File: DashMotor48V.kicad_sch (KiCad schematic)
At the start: 79 parts, among them CN3(OUT)1 XT30(2+2)PB-M.G.B, CN3(OUT)2 XT30(2+2)PB-M.G.B, J1 BM07B-SRSS-TB, J2 BM07B-SRSS-TB, Q1 FDMS039N08B, Q2 FDMS039N08B, Q3 FDMS039N08B, Q4 FDMS039N08B, Q5 FDMS039N08B, Q6 FDMS039N08B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

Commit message: Add files via upload
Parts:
- removed H1, H2, H3: MountingHole_Pad, MountingHole:MountingHole_2.2mm_M2_Pad, symbol Mechanical:MountingHole_Pad
- added H1, H2, H3: Phase A, dash:Pad_Square_Vias_6.5x6.5mm, symbol 0_connectors:Solder Pad
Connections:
- net PHASA: now also H1.1
- net PHASB: now also H2.1
- net PHASC: now also H3.1
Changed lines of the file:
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@@
 	)
 	(symbol
+		(lib_id "0_connectors:Solder Pad")
+		(at 499.11 104.14 270)
+		(unit 1)
+		(exclude_from_sim no)
+		(in_bom no)
+		(on_board yes)
+		(dnp no)
+		(property "Reference" "H3"
+			(at 503.555 97.79 90)
+			(effects
+				(font
+					(size 1.27 1.27)
+				)
+			)
+		)
+		(property "Value" "Phase A"
+			(at 503.555 100.33 90)
+			(effects
+				(font
+					(size 1.27 1.27)
+				)
+			)
+		)
+		(property "Footprint" "dash:Pad_Square_Vias_6.5x6.5mm"
+			(at 499.11 109.22 0)
+			(effects
+				(font
+					(size 1.27 1.27)
+				)
+				(hide yes)
+			)
+		)
+		(property "Datasheet" "~"
+			(at 499.11 109.22 0)
+			(effects
+				(font
+					(size 1.27 1.27)
+				)
+				(hide yes)
+			)
+		)
+		(property "Description" ""
+			(at 499.11 104.14 0)
+			(effects
+				(font
+					(size 1.27 1.27)
+				)
+				(hide yes)
+			)
+		)
+		(pin "1"
+		)
+		(instances
+			(project "DashMotor48V"
+				(path "/71f0fcc1-c7ad-470c-8d48-d038c53969d3"
+					(reference "H3")
+					(unit 1)
+				)
+			)
+		)
+	)
+	(symbol
 		(lib_id "dash:GRM32EC72A106KE05L")
 		(at 400.05 49.53 90)
@@
 	)
 	(symbol
-		(lib_id "Mechanical:MountingHole_Pad")
-		(at 499.11 101.6 0)
-		(unit 1)
-		(exclude_from_sim no)
-		(in_bom no)
-		(on_board yes)
-		(dnp no)
-		(fields_autoplaced yes)
-		(property "Reference" "H3"
-			(at 501.65 99.0599 0)
-			(effects
-				(font
-					(size 1.27 1.27)
-				)
-				(justify left)
-			)
-		)
-		(property "Value" "MountingHole_Pad"
-			(at 501.65 101.5999 0)
-			(effects
-				(font
-					(size 1.27 1.27)
-				)
-				(justify left)
-				(hide yes)
-			)
-		)
-		(property "Footprint" "MountingHole:MountingHole_2.2mm_M2_Pad"
-			(at 499.11 101.6 0)
-			(effects
-				(font
-					(size 1.27 1.27)
-				)
-				(hide yes)
-			)
-		)
-		(property "Datasheet" "~"
-			(at 499.11 101.6 0)
-			(effects
-				(font
-					(size 1.27 1.27)
-				)
-				(hide yes)
-			)
-		)
-		(property "Description" "Mounting Hole with connection"
-			(at 499.11 101.6 0)
-			(effects
-				(font
-					(size 1.27 1.27)
-				)
-				(hide yes)
-			)
-		)
-		(pin "1"
-		)
-		(instances
-			(project "DashMotor48V"
-				(path "/71f0fcc1-c7ad-470c-8d48-d038c53969d3"
-					(reference "H3")
-					(unit 1)
-				)
-			)
-		)
-	)
-	(symbol
 		(lib_id "power:+12V")
 		(at 398.78 309.88 90)
@@
 	)
 	(symbol
-		(lib_id "Mechanical:MountingHole_Pad")
-		(at 411.48 101.6 0)
+		(lib_id "power:PWR_FLAG")
+		(at 398.78 340.36 270)
 		(unit 1)
 		(exclude_from_sim no)
-		(in_bom no)
+		(in_bom yes)
 		(on_board yes)
 		(dnp no)
 		(fields_autoplaced yes)
-		(property "Reference" "H1"
-			(at 414.02 99.0599 0)
+		(property "Reference" "#FLG05"
+			(at 400.685 340.36 0)
 			(effects
 				(font
 					(size 1.27 1.27)
 				)
-				(justify left)
+				(hide yes)
 			)
 		)
-		(property "Value" "MountingHole_Pad"
-			(at 414.02 101.5999 0)
+		(property "Value" "PWR_FLAG"
+			(at 403.86 340.36 0)
 			(effects
 				(font
 					(size 1.27 1.27)
 				)
-				(justify left)
-				(hide yes)
 			)
 		)
-		(property "Footprint" "MountingHole:MountingHole_2.2mm_M2_Pad"
-			(at 411.48 101.6 0)
+		(property "Footprint" ""
+			(at 398.78 340.36 0)
 			(effects
 				(font
@@
 		)
 		(property "Datasheet" "~"
-			(at 411.48 101.6 0)
+			(at 398.78 340.36 0)
 			(effects
 				(font
@@
 			)
 		)
-		(property "Description" "Mounting Hole with connection"
-			(at 411.48 101.6 0)
+		(property "Description" "Special symbol for telling ERC where power comes from"
+			(at 398.78 340.36 0)
 			(effects
 				(font
@@
 		)
 		(instances
-			(project ""
+			(project "DashMotor48V"
 				(path "/71f0fcc1-c7ad-470c-8d48-d038c53969d3"
-					(reference "H1")
+					(reference "#FLG05")
 					(unit 1)
 				)
@@
 	)
 	(symbol
-		(lib_id "power:PWR_FLAG")
-		(at 398.78 340.36 270)
+		(lib_id "0_connectors:Solder Pad")
+		(at 454.66 104.14 270)
 		(unit 1)
 		(exclude_from_sim no)
-		(in_bom yes)
+		(in_bom no)
 		(on_board yes)
 		(dnp no)
-		(fields_autoplaced yes)
-		(property "Reference" "#FLG05"
-			(at 400.685 340.36 0)
+		(property "Reference" "H2"
+			(at 459.105 97.79 90)
 			(effects
 				(font
 					(size 1.27 1.27)
 				)
-				(hide yes)
 			)
 		)
-		(property "Value" "PWR_FLAG"
-			(at 403.86 340.36 0)
+		(property "Value" "Phase A"
+			(at 459.105 100.33 90)
 			(effects
 				(font
@@
 			)
 		)
-		(property "Footprint" ""
-			(at 398.78 340.36 0)
+		(property "Footprint" "dash:Pad_Square_Vias_6.5x6.5mm"
+			(at 454.66 109.22 0)
 			(effects
 				(font
@@
 		)
 		(property "Datasheet" "~"
-			(at 398.78 340.36 0)
+			(at 454.66 109.22 0)
 			(effects
 				(font
@@
 			)
 		)
-		(property "Description" "Special symbol for telling ERC where power comes from"
-			(at 398.78 340.36 0)
+		(property "Description" ""
+			(at 454.66 104.14 0)
 			(effects
 				(font
@@
 			(project "DashMotor48V"
 				(path "/71f0fcc1-c7ad-470c-8d48-d038c53969d3"
-					(reference "#FLG05")
+					(reference "H2")
 					(unit 1)
 				)
@@
 	)
 	(symbol
-		(lib_id "Mechanical:MountingHole_Pad")
-		(at 454.66 101.6 0)
-		(unit 1)
-		(exclude_from_sim no)
-		(in_bom no)
-		(on_board yes)
-		(dnp no)
-		(fields_autoplaced yes)
-		(property "Reference" "H2"
-			(at 457.2 99.0599 0)
-			(effects
-				(font
-					(size 1.27 1.27)
-				)
-				(justify left)
-			)
-		)
-		(property "Value" "MountingHole_Pad"
-			(at 457.2 101.5999 0)
-			(effects
-				(font
-					(size 1.27 1.27)
-				)
-				(justify left)
-				(hide yes)
-			)
-		)
-		(property "Footprint" "MountingHole:MountingHole_2.2mm_M2_Pad"
-			(at 454.66 101.6 0)
-			(effects
-				(font
-					(size 1.27 1.27)
-				)
-				(hide yes)
-			)
-		)
-		(property "Datasheet" "~"
-			(at 454.66 101.6 0)
-			(effects
-				(font
-					(size 1.27 1.27)
-				)
-				(hide yes)
-			)
-		)
-		(property "Description" "Mounting Hole with connection"
-			(at 454.66 101.6 0)
-			(effects
-				(font
-					(size 1.27 1.27)
-				)
-				(hide yes)
-			)
-		)
-		(pin "1"
-		)
-		(instances
-			(project "DashMotor48V"
-				(path "/71f0fcc1-c7ad-470c-8d48-d038c53969d3"
-					(reference "H2")
-					(unit 1)
-				)
-			)
-		)
-	)
-	(symbol
 		(lib_id "dash:FDMS039N08B")
 		(at 487.68 123.19 0)
@@
 					(unit 1)
 				)
+			)
+		)
+	)
+	(symbol
+		(lib_id "0_connectors:Solder Pad")
+		(at 411.48 104.14 270)
+		(unit 1)
+		(exclude_from_sim no)
+		(in_bom no)
+		(on_board yes)
+		(dnp no)
+		(property "Reference" "H1"
+			(at 415.925 97.79 90)
+			(effects
+				(font
+					(size 1.27 1.27)
+				)
+			)
+		)
+		(property "Value" "Phase A"
+			(at 415.925 100.33 90)
+			(effects
+				(font
+					(size 1.27 1.27)
+				)
+			)
+		)
+		(property "Footprint" "dash:Pad_Square_Vias_6.5x6.5mm"
+			(at 411.48 109.22 0)
+			(effects
+				(font
+					(size 1.27 1.27)
+				)
+				(hide yes)
+			)
+		)
+		(property "Datasheet" "~"
+			(at 411.48 109.22 0)
+			(effects
+				(font
+					(size 1.27 1.27)
+				)
+				(hide yes)
+			)
+		)
+		(property "Description" ""
+			(at 411.48 104.14 0)
+			(effects
+				(font
+					(size 1.27 1.27)
+				)
+				(hide yes)
+			)
+		)
+		(pin "1"
+		)
+		(instances
+			(project "DashMotor48V"
+				(path "/71f0fcc1-c7ad-470c-8d48-d038c53969d3"
+					(reference "H1")
+					(unit 1)
+				)

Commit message: change color and stuff
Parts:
- added H4, H5, H6, H7: MountingHole, MountingHole:MountingHole_2.2mm_M2_Pad, symbol Mechanical:MountingHole

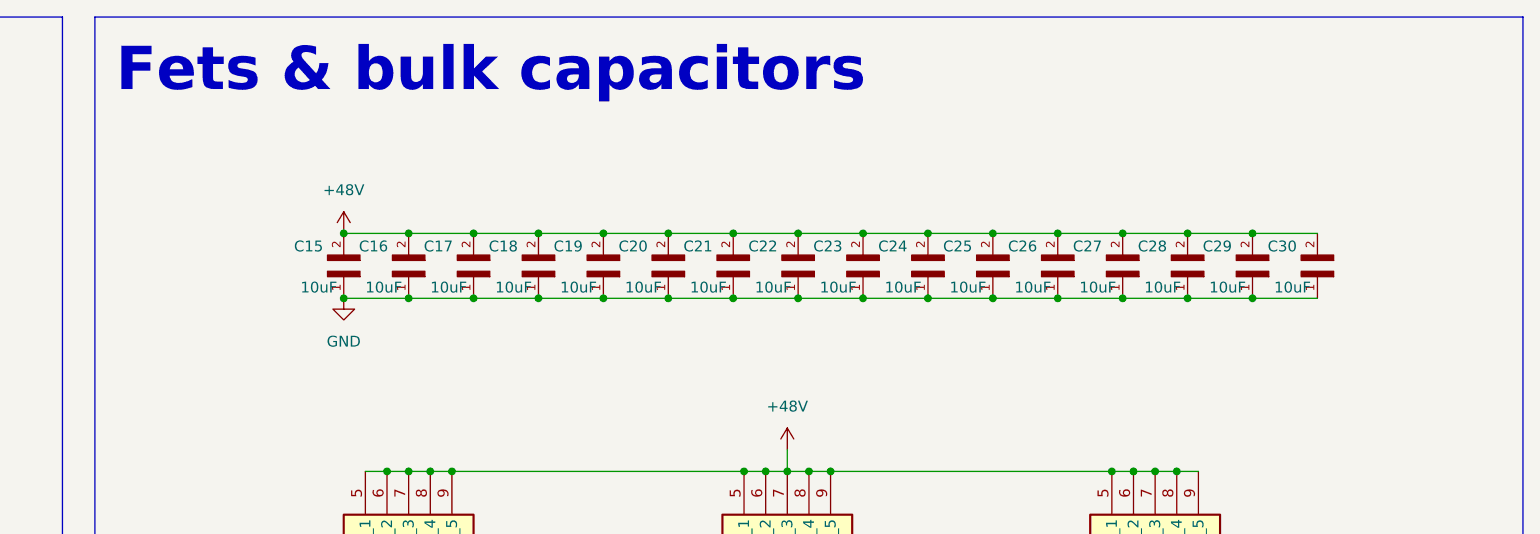
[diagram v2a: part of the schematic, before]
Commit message: need to add testing probe
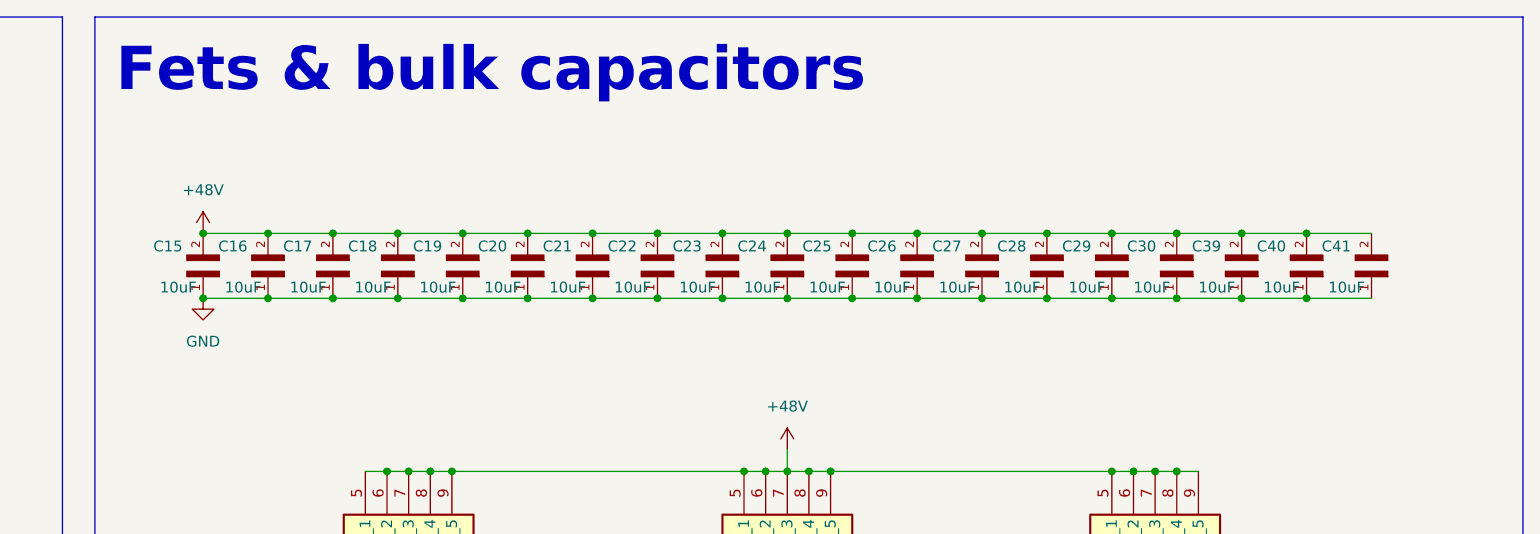
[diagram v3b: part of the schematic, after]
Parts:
- added C39, C40, C41: 10uF, dash:GRM32EC72A106KE05L, symbol dash:GRM32EC72A106KE05L
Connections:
- net +48V: now also C39.2, C40.2, C41.2
- net GND: now also C39.1, C40.1, C41.1
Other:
- moved on the sheet: C15, C16, C17, C18, C19, C20, C21, C22, C23, C24, C25, C26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

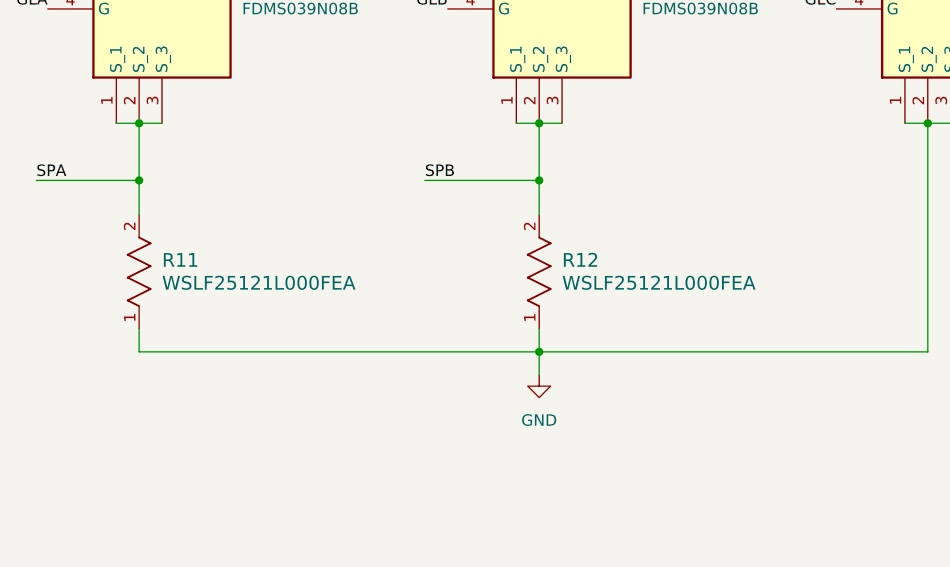
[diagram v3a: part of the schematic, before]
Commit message: change a smaller shunt resistor and add more ground vias
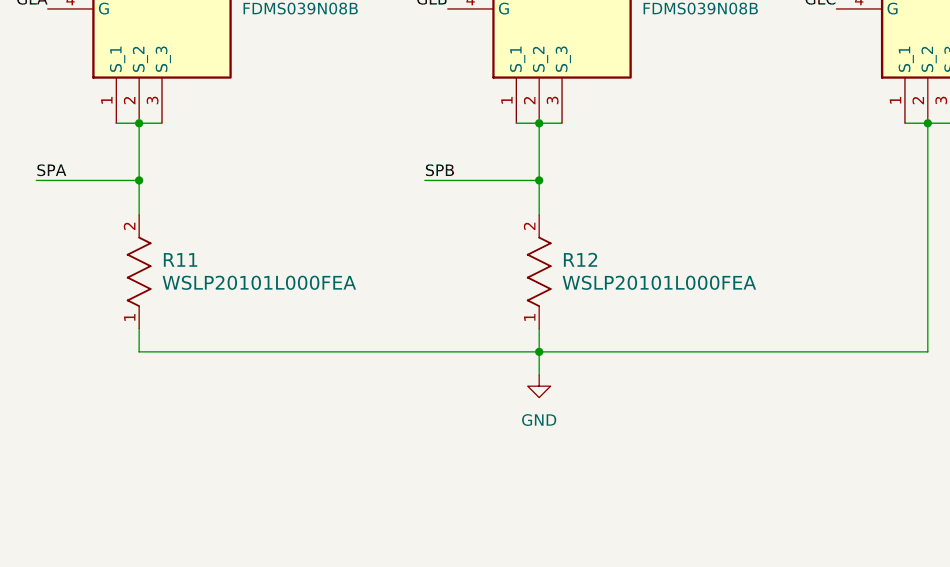
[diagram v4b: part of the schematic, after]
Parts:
- removed R11, R12: WSLF25121L000FEA, dash:WSLF25121L000FEA, symbol dash:WSLF25121L000FEA
- added R11, R12: WSLP20101L000FEA, dash:WSLP20101L000FEA, symbol dash:WSLP20101L000FEA
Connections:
- net GND: now also R11.1, R12.1
- net SPA: now also R11.2
- net SPB: now also R12.2
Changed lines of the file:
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@@
 	)
 	(symbol
+		(lib_id "dash:WSLP20101L000FEA")
+		(at 397.51 158.75 90)
+		(unit 1)
+		(exclude_from_sim no)
+		(in_bom yes)
+		(on_board yes)
+		(dnp no)
+		(fields_autoplaced yes)
+		(property "Reference" "R11"
+			(at 400.05 151.1299 90)
+			(effects
+				(font
+					(size 1.524 1.524)
+				)
+				(justify right)
+			)
+		)
+		(property "Value" "WSLP20101L000FEA"
+			(at 400.05 153.6699 90)
+			(effects
+				(font
+					(size 1.524 1.524)
+				)
+				(justify right)
+			)
+		)
+		(property "Footprint" "dash:WSLP20101L000FEA"
+			(at 397.51 158.75 0)
+			(effects
+				(font
+					(size 1.27 1.27)
+					(italic yes)
+				)
+				(hide yes)
+			)
+		)
+		(property "Datasheet" "https://www.vishay.com/doc?30122"
+			(at 397.51 158.75 0)
+			(effects
+				(font
+					(size 1.27 1.27)
+					(italic yes)
+				)
+				(hide yes)
+			)
+		)
+		(property "Description" ""
+			(at 397.51 158.75 0)
+			(effects
+				(font
+					(size 1.27 1.27)
+				)
+				(hide yes)
+			)
+		)
+		(pin "1"
+		)
+		(pin "2"
+		)
+		(instances
+			(project ""
+				(path "/71f0fcc1-c7ad-470c-8d48-d038c53969d3"
+					(reference "R11")
+					(unit 1)
+				)
+			)
+		)
+	)
+	(symbol
 		(lib_id "dash:CC0603JRX7R9BB104")
 		(at 118.11 166.37 270)
@@
 	)
 	(symbol
+		(lib_id "dash:WSLP20101L000FEA")
+		(at 441.96 158.75 90)
+		(unit 1)
+		(exclude_from_sim no)
+		(in_bom yes)
+		(on_board yes)
+		(dnp no)
+		(fields_autoplaced yes)
+		(property "Reference" "R12"
+			(at 444.5 151.1299 90)
+			(effects
+				(font
+					(size 1.524 1.524)
+				)
+				(justify right)
+			)
+		)
+		(property "Value" "WSLP20101L000FEA"
+			(at 444.5 153.6699 90)
+			(effects
+				(font
+					(size 1.524 1.524)
+				)
+				(justify right)
+			)
+		)
+		(property "Footprint" "dash:WSLP20101L000FEA"
+			(at 441.96 158.75 0)
+			(effects
+				(font
+					(size 1.27 1.27)
+					(italic yes)
+				)
+				(hide yes)
+			)
+		)
+		(property "Datasheet" "https://www.vishay.com/doc?30122"
+			(at 441.96 158.75 0)
+			(effects
+				(font
+					(size 1.27 1.27)
+					(italic yes)
+				)
+				(hide yes)
+			)
+		)
+		(property "Description" ""
+			(at 441.96 158.75 0)
+			(effects
+				(font
+					(size 1.27 1.27)
+				)
+				(hide yes)
+			)
+		)
+		(pin "1"
+		)
+		(pin "2"
+		)
+		(instances
+			(project "DashMotor48V"
+				(path "/71f0fcc1-c7ad-470c-8d48-d038c53969d3"
+					(reference "R12")
+					(unit 1)
+				)
+			)
+		)
+	)
+	(symbol
 		(lib_id "power:GND")
 		(at 441.96 163.83 0)
@@
 	)
 	(symbol
-		(lib_id "dash:WSLF25121L000FEA")
-		(at 441.96 158.75 90)
-		(unit 1)
-		(exclude_from_sim no)
-		(in_bom yes)
-		(on_board yes)
-		(dnp no)
-		(fields_autoplaced yes)
-		(property "Reference" "R12"
-			(at 444.5 151.1299 90)
-			(effects
-				(font
-					(size 1.524 1.524)
-				)
-				(justify right)
-			)
-		)
-		(property "Value" "WSLF25121L000FEA"
-			(at 444.5 153.6699 90)
-			(effects
-				(font
-					(size 1.524 1.524)
-				)
-				(justify right)
-			)
-		)
-		(property "Footprint" "dash:WSLF25121L000FEA"
-			(at 441.96 158.75 0)
-			(effects
-				(font
-					(size 1.27 1.27)
-					(italic yes)
-				)
-				(hide yes)
-			)
-		)
-		(property "Datasheet" "https://www.vishay.com/doc?30193"
-			(at 441.96 158.75 0)
-			(effects
-				(font
-					(size 1.27 1.27)
-					(italic yes)
-				)
-				(hide yes)
-			)
-		)
-		(property "Description" ""
-			(at 441.96 158.75 0)
-			(effects
-				(font
-					(size 1.27 1.27)
-				)
-				(hide yes)
-			)
-		)
-		(pin "1"
-		)
-		(pin "2"
-		)
-		(instances
-			(project "DashMotor48V"
-				(path "/71f0fcc1-c7ad-470c-8d48-d038c53969d3"
-					(reference "R12")
-					(unit 1)
-				)
-			)
-		)
-	)
-	(symbol
 		(lib_id "dash:GRM155R60J475ME87D")
 		(at 67.31 124.46 90)
@@
 					(unit 1)
 				)
-			)
-		)
-	)
-	(symbol
-		(lib_id "dash:WSLF25121L000FEA")
-		(at 397.51 158.75 90)
-		(unit 1)
-		(exclude_from_sim no)
-		(in_bom yes)
-		(on_board yes)
-		(dnp no)
-		(fields_autoplaced yes)
-		(property "Reference" "R11"
-			(at 400.05 151.1299 90)
-			(effects
-				(font
-					(size 1.524 1.524)
-				)
-				(justify right)
-			)
-		)
-		(property "Value" "WSLF25121L000FEA"
-			(at 400.05 153.6699 90)
-			(effects
-				(font
-					(size 1.524 1.524)
-				)
-				(justify right)
-			)
-		)
-		(property "Footprint" "dash:WSLF25121L000FEA"
-			(at 397.51 158.75 0)
-			(effects
-				(font
-					(size 1.27 1.27)
-					(italic yes)
-				)
-				(hide yes)
-			)
-		)
-		(property "Datasheet" "https://www.vishay.com/doc?30193"
-			(at 397.51 158.75 0)
-			(effects
-				(font
-					(size 1.27 1.27)
-					(italic yes)
-				)
-				(hide yes)
-			)
-		)
-		(property "Description" ""
-			(at 397.51 158.75 0)
-			(effects
-				(font
-					(size 1.27 1.27)
-				)
-				(hide yes)
-			)
-		)
-		(pin "1"
-		)
-		(pin "2"
-		)
-		(instances
-			(project ""
-				(path "/71f0fcc1-c7ad-470c-8d48-d038c53969d3"
-					(reference "R11")
-					(unit 1)
-				)
